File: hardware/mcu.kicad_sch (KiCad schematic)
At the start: 18 parts, among them U1 RP2350B, U2 W25Q128JVS, Y1 12MHz

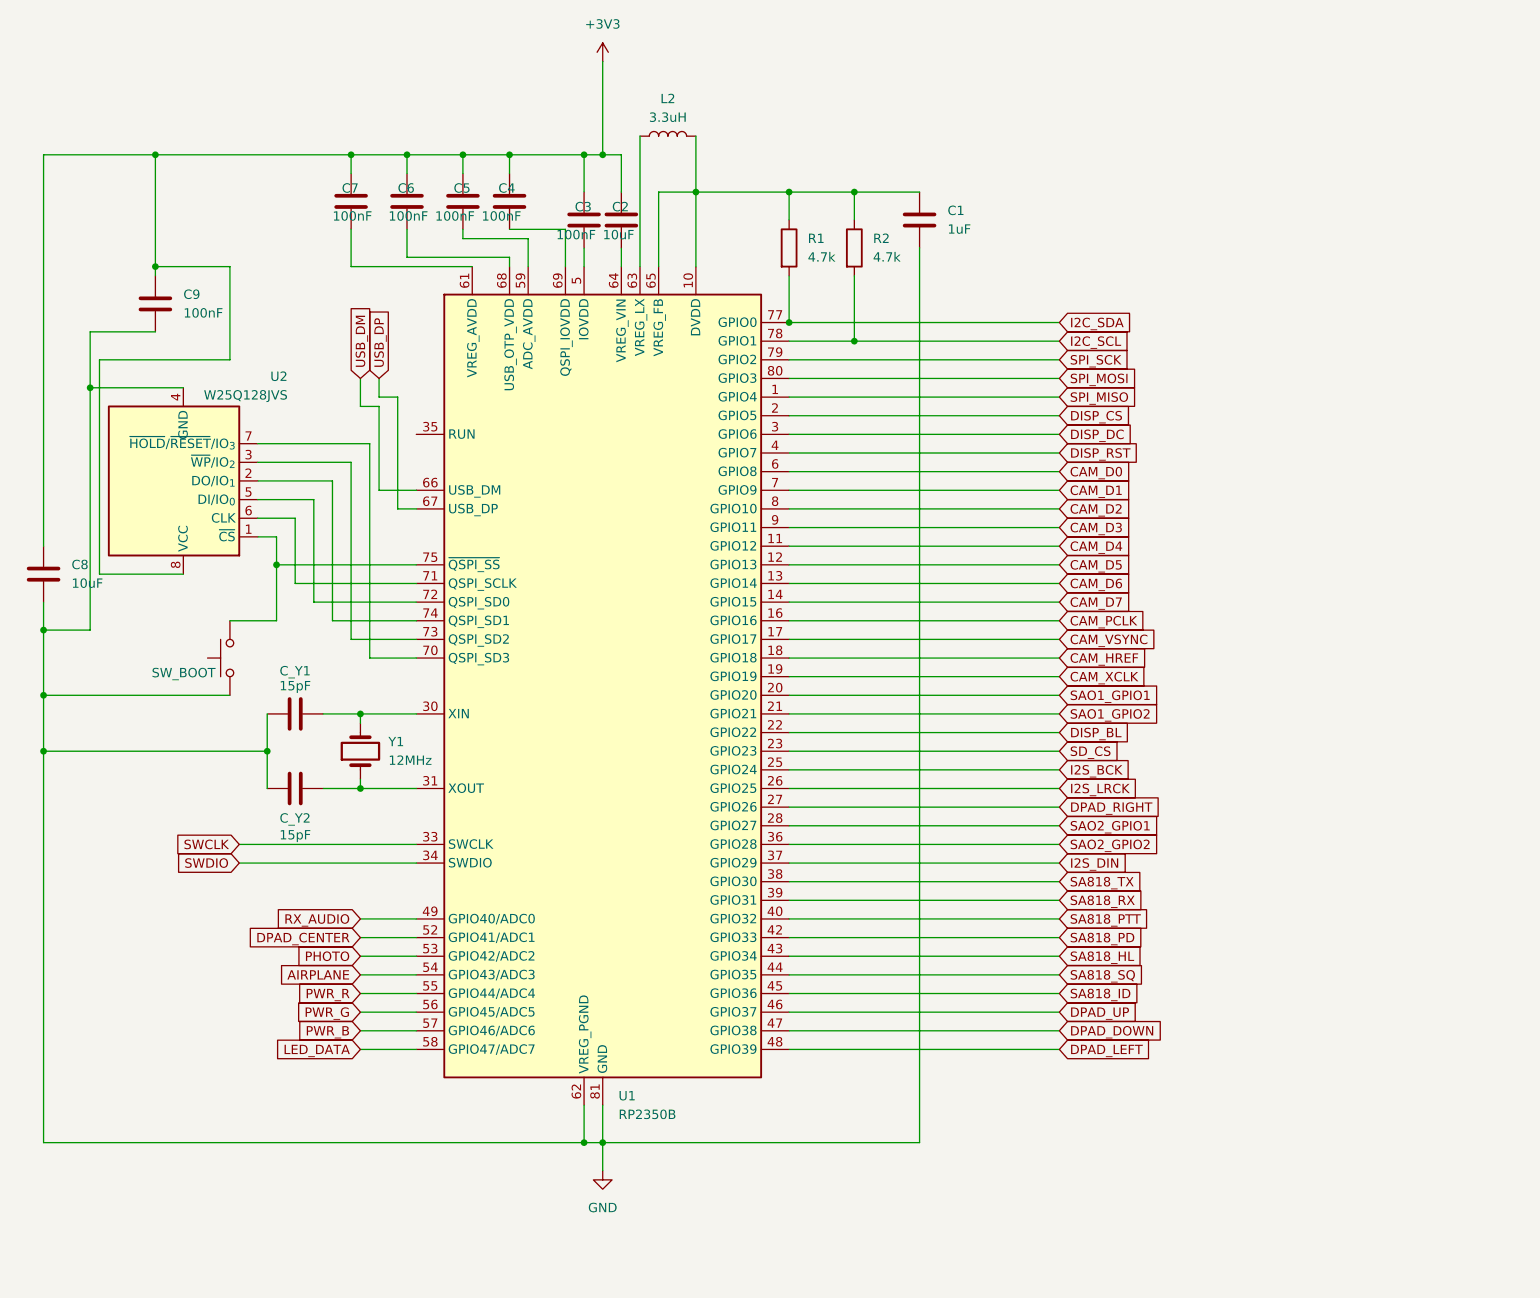
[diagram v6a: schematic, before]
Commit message: all design sheets complete, ERC clean
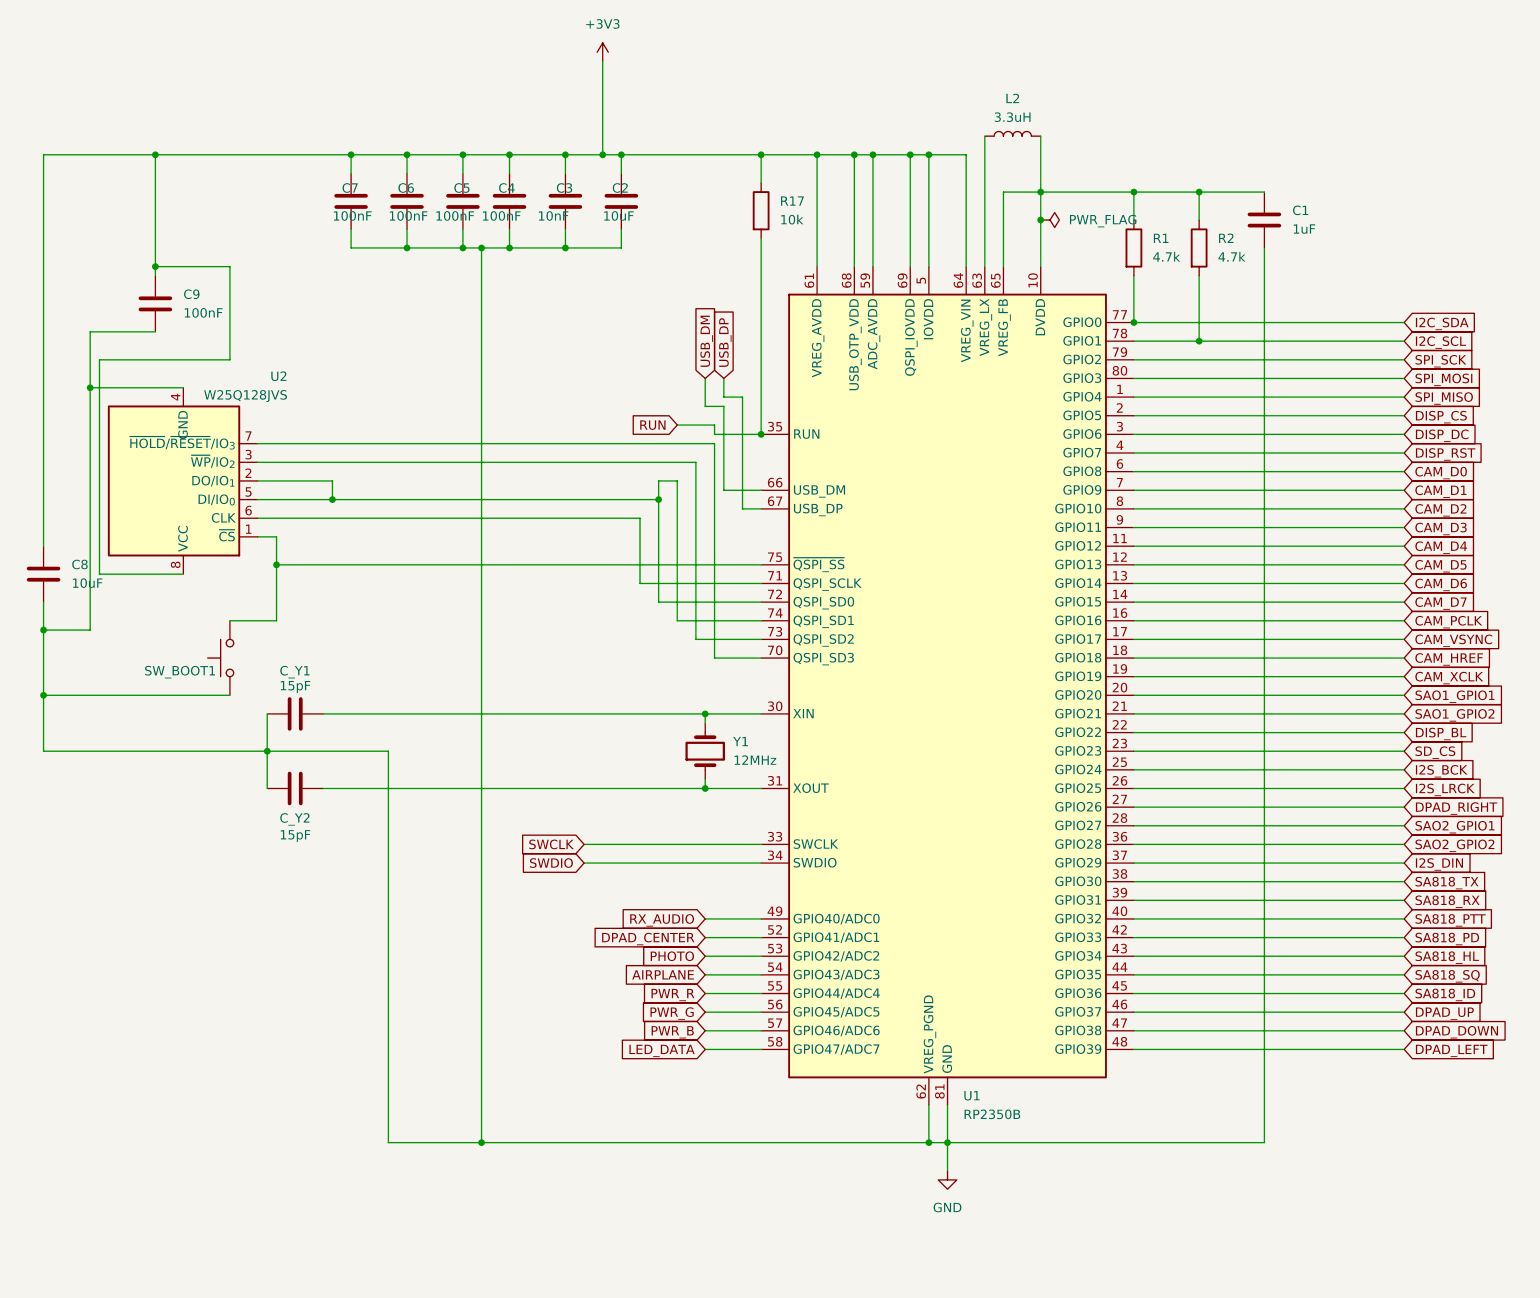
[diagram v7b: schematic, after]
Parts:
- added R17: 10k, symbol Device:R
- C3: value 100nF -> 10nF
- renumbered SW_BOOT to SW_BOOT1
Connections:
- net +3V3: now also U1.15 (IOVDD), U1.24 (IOVDD), U1.29 (IOVDD), U1.41 (IOVDD), U1.5 (IOVDD), U1.50 (IOVDD), U1.59 (ADC_AVDD), U1.60 (IOVDD), U1.61 (VREG_AVDD), U1.64 (VREG_VIN), U1.68 (USB_OTP_VDD), U1.69 (QSPI_IOVDD), U1.76 (IOVDD), R17.1
- net GND: now also C2.2, C3.2, C4.2, C5.2, C6.2, C7.2
- net RUN: now reaches U1.35 (RUN)
- net RUN: now also R17.2
- net at U1.72 (QSPI_SD0), U2.5 (DI/IO_{0}): now also U1.74 (QSPI_SD1), U2.2 (DO/IO_{1})
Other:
- moved on the sheet: C1, C2, C3, L2, R1, R2, U1, Y1
